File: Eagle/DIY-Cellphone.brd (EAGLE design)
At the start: 130.8 x 58.4 mm, 66 parts, among them IC1 MEGA1284, J1 ISP, U1 MCP73831, U7 M10_HDWITHOUT_EXCLUSION, X1 BU-SMA-V, X3 CCM03-3002 R102

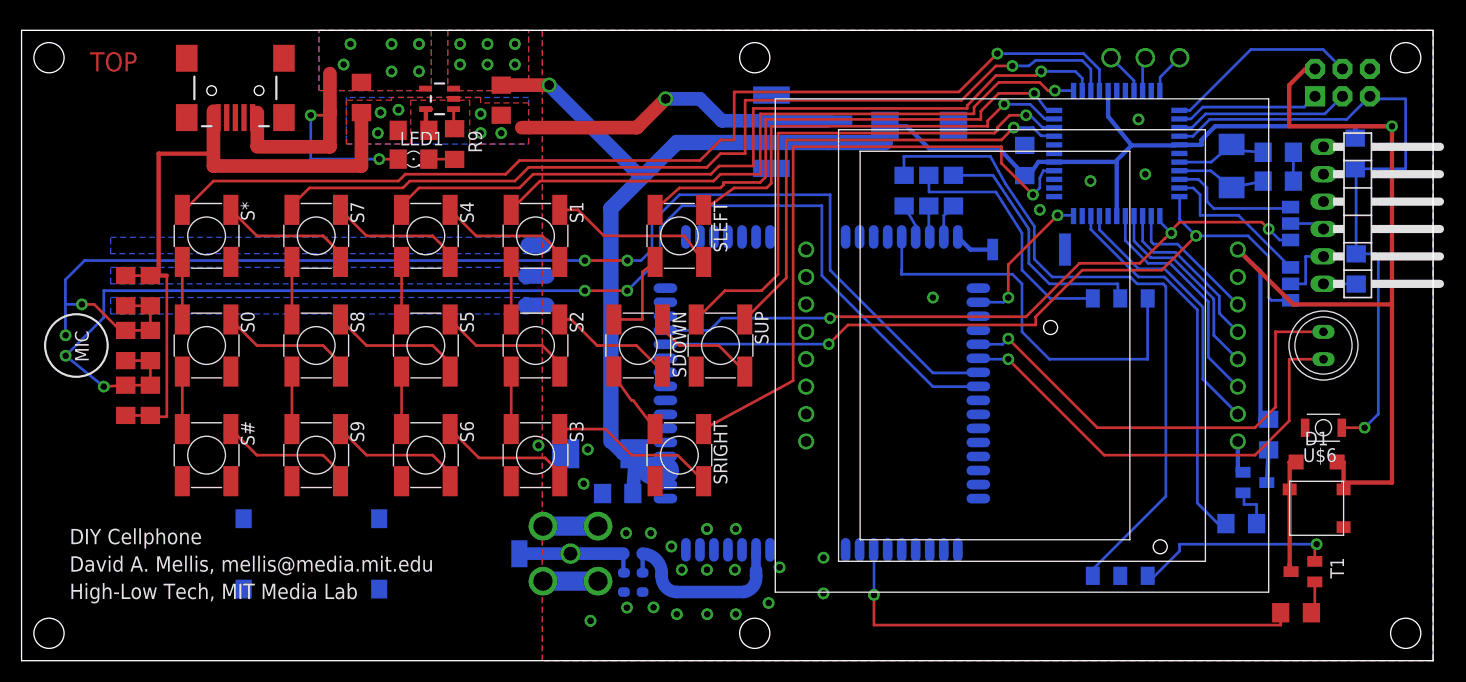
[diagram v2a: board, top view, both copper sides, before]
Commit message: Reverting to two caps. Labeling FTDI header colors.
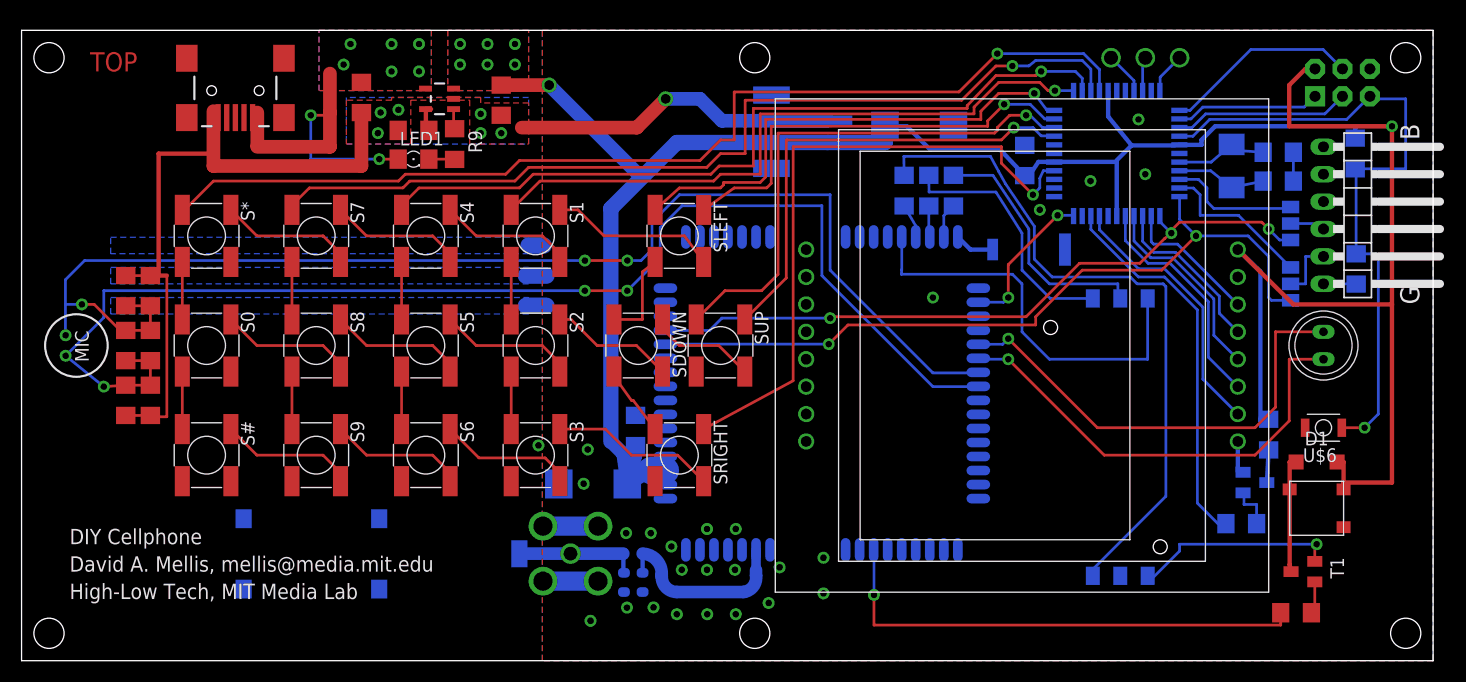
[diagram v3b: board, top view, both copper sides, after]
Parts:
- moved C13 6.07 mm to (56.9, 21.3), turned to 90 degrees
- moved C16 2.87 mm to (53.0, 16.4)
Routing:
- net VCC: track 239.2 -> 241.3 mm
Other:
- board text added: "B"
- board text added: "G"
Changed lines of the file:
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@@
 <text x="116.205" y="34.925" size="1.016" layer="26" font="fixed" rot="MR270">Cell</text>
 <text x="6.35" y="54.61" size="1.778" layer="1">TOP</text>
+<text x="129.54" y="48.26" size="1.778" layer="25" rot="R90">B</text>
+<text x="129.54" y="33.02" size="1.778" layer="25" rot="R90">G</text>
 </plain>
 <attributes>
@@
 </element>
 <element name="R4" library="rcl" package="R1206" value="10K" x="123.59" y="47.006" smashed="yes" rot="MR90">
-<attribute name="VALUE" x="121.304" y="45.609" size="1.016" layer="28" rot="MR90"/>
+<attribute name="VALUE" x="125.114" y="45.609" size="1.016" layer="28" rot="MR90"/>
 </element>
 <element name="C1" library="rcl" package="C1206" value="100 nF" x="123.679" y="36.306" smashed="yes" rot="MR90">
-<attribute name="VALUE" x="121.647" y="34.655" size="1.016" layer="28" rot="MR90"/>
+<attribute name="VALUE" x="125.457" y="34.02" size="1.016" layer="28" rot="MR90"/>
 </element>
 <element name="S1" library="cellphone" package="BUTTON_6MM_JLEAD" value="" x="47.625" y="39.37" rot="R270"/>
@@
 <attribute name="VALUE" x="86.2" y="52.305" size="1.016" layer="28" rot="MR0"/>
 </element>
-<element name="C13" library="rcl" package="C1206" value="0.1uF" x="55.245" y="15.494" smashed="yes" rot="MR0">
-<attribute name="VALUE" x="57.404" y="16.51" size="1.016" layer="28" rot="MR0"/>
+<element name="C13" library="rcl" package="C1206" value="0.1uF" x="56.896" y="21.336" smashed="yes" rot="MR90">
+<attribute name="VALUE" x="57.912" y="19.177" size="1.016" layer="28" rot="MR90"/>
 </element>
 <element name="C12" library="rcl" package="C1206" value="0.1uF" x="92.964" y="46.355" smashed="yes" rot="MR90">
@@
 <element name="U$4" library="cellphone" package="414-VA5R" value="SUPERCAPPAS" x="93.345" y="38.1" rot="MR180"/>
 <element name="8MHZ" library="fab" package="2-SMD-5X3MM" value="CRYSTAL" x="112.141" y="45.847" smashed="yes" rot="MR90">
-<attribute name="NAME" x="114.808" y="41.021" size="1.016" layer="26" rot="MR0"/>
+<attribute name="NAME" x="112.903" y="41.021" size="1.016" layer="26" rot="MR0"/>
 </element>
 <element name="C14" library="rcl" package="C1206" value="18pF" x="116.459" y="44.45" smashed="yes" rot="MR180">
@@
 <attribute name="VALUE" x="117.602" y="35.0251" size="0.02" layer="28" rot="MR270"/>
 </element>
-<element name="C16" library="rcl" package="D/7343-31R" value="1000uF" x="53.594" y="19.177" smashed="yes" rot="MR180">
-<attribute name="VALUE" x="50.579" y="22.498" size="1.016" layer="28" rot="MR180"/>
+<element name="C16" library="rcl" package="D/7343-31R" value="1000uF" x="52.959" y="16.383" smashed="yes" rot="MR180">
+<attribute name="VALUE" x="49.944" y="19.704" size="1.016" layer="28" rot="MR180"/>
 </element>
 <element name="U$5" library="cellphone" package="SPEAKER-6.4MM" value="MINI-SIREN" x="120.65" y="29.21" rot="R270"/>
@@
 <contactref element="C16" pad="+"/>
 <wire x1="54.61" y1="20.32" x2="55.753" y2="19.177" width="1.27" layer="16"/>
-<wire x1="55.753" y1="19.177" x2="56.769" y2="19.177" width="1.27" layer="16"/>
-<wire x1="56.769" y1="19.177" x2="56.896" y2="19.05" width="1.27" layer="16"/>
-<wire x1="56.896" y1="19.05" x2="56.645" y2="15.494" width="1.27" layer="16"/>
-<wire x1="56.769" y1="19.177" x2="58.322" y2="17.624" width="1.27" layer="16"/>
+<wire x1="55.753" y1="19.177" x2="56.134" y2="16.383" width="1.27" layer="16"/>
+<wire x1="56.134" y1="16.383" x2="56.896" y2="19.05" width="1.27" layer="16"/>
+<wire x1="56.896" y1="19.05" x2="56.896" y2="19.936" width="1.27" layer="16"/>
+<wire x1="56.134" y1="16.383" x2="58.322" y2="17.624" width="1.27" layer="16"/>
 <wire x1="58.322" y1="17.624" x2="59.665" y2="17.624" width="2.54" layer="16"/>
 <wire x1="59.665" y1="18.924" x2="59.665" y2="17.624" width="0.4064" layer="16"/>

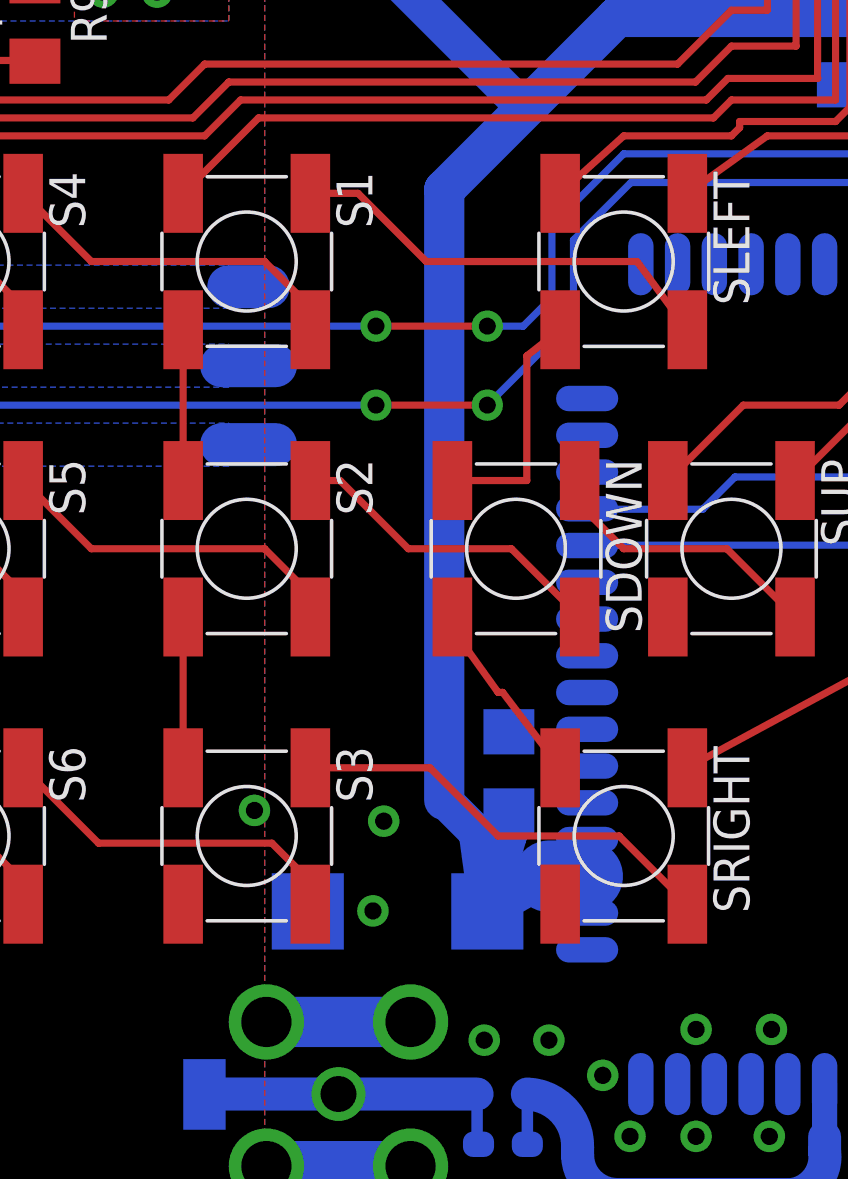
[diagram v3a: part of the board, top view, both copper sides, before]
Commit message: Moving capacitors (near the cellular module).
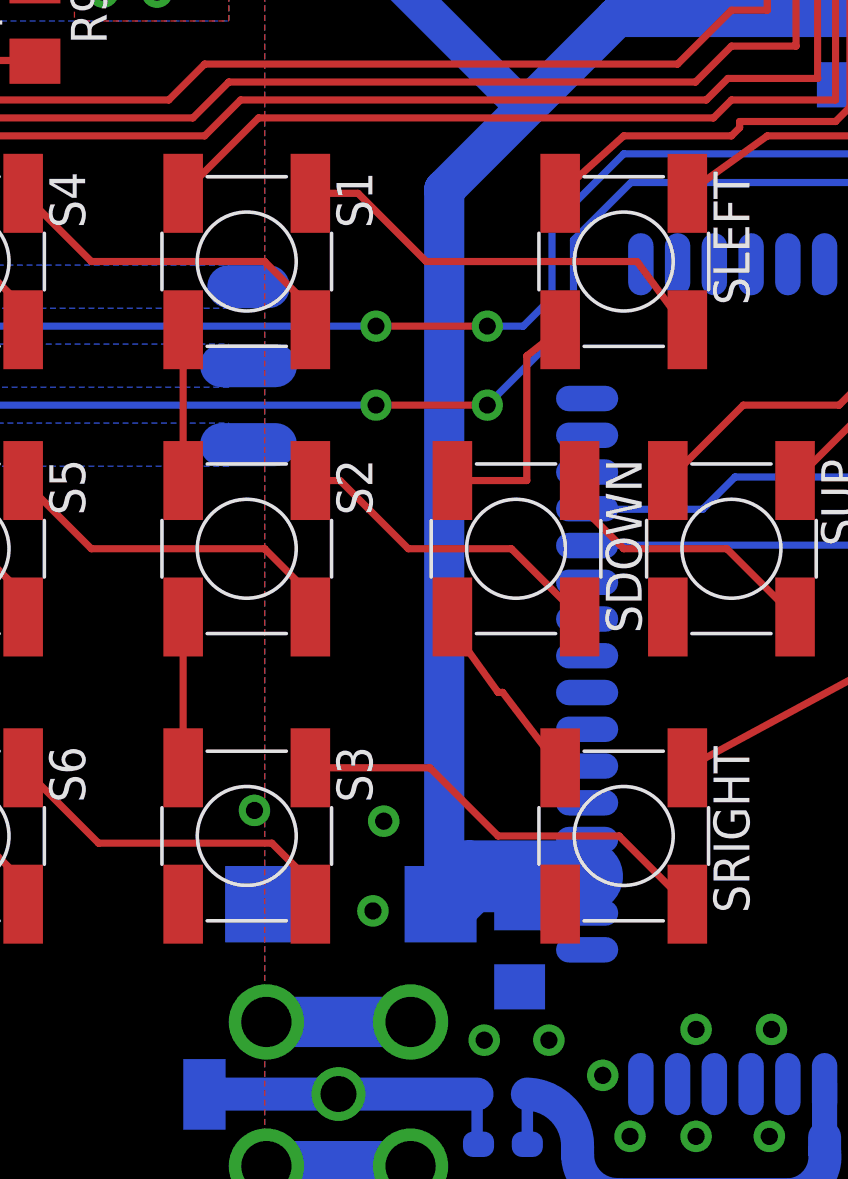
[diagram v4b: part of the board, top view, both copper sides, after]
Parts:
- moved C13 6.23 mm to (57.3, 15.1), turned to 270 degrees
- moved C16 1.67 mm to (51.3, 16.6)
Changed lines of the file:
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@@
 <attribute name="VALUE" x="86.2" y="52.305" size="1.016" layer="28" rot="MR0"/>
 </element>
-<element name="C13" library="rcl" package="C1206" value="0.1uF" x="56.896" y="21.336" smashed="yes" rot="MR90">
-<attribute name="VALUE" x="57.912" y="19.177" size="1.016" layer="28" rot="MR90"/>
+<element name="C13" library="rcl" package="C1206" value="0.1uF" x="57.277" y="15.113" smashed="yes" rot="MR270">
+<attribute name="VALUE" x="56.261" y="17.272" size="1.016" layer="28" rot="MR270"/>
 </element>
 <element name="C12" library="rcl" package="C1206" value="0.1uF" x="92.964" y="46.355" smashed="yes" rot="MR90">
@@
 <attribute name="VALUE" x="117.602" y="35.0251" size="0.02" layer="28" rot="MR270"/>
 </element>
-<element name="C16" library="rcl" package="D/7343-31R" value="1000uF" x="52.959" y="16.383" smashed="yes" rot="MR180">
-<attribute name="VALUE" x="49.944" y="19.704" size="1.016" layer="28" rot="MR180"/>
+<element name="C16" library="rcl" package="D/7343-31R" value="1000uF" x="51.308" y="16.637" smashed="yes" rot="MR180">
+<attribute name="VALUE" x="48.293" y="19.958" size="1.016" layer="28" rot="MR180"/>
 </element>
 <element name="U$5" library="cellphone" package="SPEAKER-6.4MM" value="MINI-SIREN" x="120.65" y="29.21" rot="R270"/>
@@
 <wire x1="74.693" y1="48.022" x2="60.722" y2="48.022" width="1.4224" layer="16"/>
 <wire x1="60.722" y1="48.022" x2="54.61" y2="41.91" width="1.4224" layer="16"/>
-<wire x1="54.61" y1="41.91" x2="54.61" y2="20.32" width="1.4224" layer="16"/>
+<wire x1="54.61" y1="41.91" x2="54.61" y2="16.764" width="1.4224" layer="16"/>
 <wire x1="127" y1="49.53" x2="127" y2="33.02" width="0.4064" layer="1"/>
 <wire x1="127" y1="33.02" x2="117.856" y2="33.02" width="0.4064" layer="1"/>
@@
 <wire x1="107.292" y1="47.806" x2="109.347" y2="47.806" width="0.4064" layer="16"/>
 <contactref element="C16" pad="+"/>
-<wire x1="54.61" y1="20.32" x2="55.753" y2="19.177" width="1.27" layer="16"/>
-<wire x1="55.753" y1="19.177" x2="56.134" y2="16.383" width="1.27" layer="16"/>
-<wire x1="56.134" y1="16.383" x2="56.896" y2="19.05" width="1.27" layer="16"/>
-<wire x1="56.896" y1="19.05" x2="56.896" y2="19.936" width="1.27" layer="16"/>
-<wire x1="56.134" y1="16.383" x2="58.322" y2="17.624" width="1.27" layer="16"/>
-<wire x1="58.322" y1="17.624" x2="59.665" y2="17.624" width="2.54" layer="16"/>
 <wire x1="59.665" y1="18.924" x2="59.665" y2="17.624" width="0.4064" layer="16"/>
 <wire x1="59.665" y1="17.624" x2="59.665" y2="16.324" width="0.4064" layer="16"/>
@@
 <via x="43.18" y="55.245" extent="1-16" drill="0.6"/>
 <via x="45.72" y="55.245" extent="1-16" drill="0.6"/>
+<wire x1="54.61" y1="16.764" x2="54.483" y2="16.637" width="1.4224" layer="16"/>
+<wire x1="54.61" y1="16.764" x2="55.47" y2="17.624" width="2.54" layer="16"/>
+<wire x1="55.47" y1="17.624" x2="59.665" y2="17.624" width="2.54" layer="16"/>
+<wire x1="57.277" y1="16.513" x2="58.388" y2="17.624" width="1.4224" layer="16"/>
+<wire x1="58.388" y1="17.624" x2="59.665" y2="17.624" width="1.4224" layer="16"/>
 </signal>
 <signal name="ANT" class="4">

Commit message: Add LED on M10 status pin.
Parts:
- added LED2: (no value), led:1206
- added R10: 470, rcl:R1206
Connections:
- new net N$37: LED2.C, R10.1
- net GND: now also R10.2
- net STATUS: now also LED2.A
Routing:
- net STATUS: track 3.84 -> 28.0 mm
- net N$37: track 0.00 -> 3.81 mm
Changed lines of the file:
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@@
 <element name="JP3" library="SparkFun-Connectors" package="JST-2-SMD" value="" x="70.993" y="49.022" rot="MR270"/>
 <element name="U1" library="SparkFun" package="SOT23-5" value="MCP73831" x="38.735" y="52.07" smashed="yes" rot="R90">
-<attribute name="VALUE" x="40.3225" y="54.1655" size="0.4064" layer="27" rot="R180"/>
+<attribute name="VALUE" x="41.5925" y="54.1655" size="0.8128" layer="27" rot="R180"/>
 </element>
 <element name="R7" library="rcl" package="R1206" value="2K" x="36.322" y="49.149" smashed="yes" rot="R180">
-<attribute name="VALUE" x="36.957" y="47.879" size="0.8128" layer="27" rot="R180"/>
+<attribute name="VALUE" x="36.957" y="51.054" size="0.8128" layer="27" rot="R180"/>
 </element>
 <element name="C3" library="rcl" package="C1206" value="4.7uF" x="31.496" y="52.197" smashed="yes" rot="R270">
@@
 </element>
 <element name="C4" library="rcl" package="C1206" value="4.7uF" x="44.45" y="51.943" smashed="yes" rot="R270">
-<attribute name="VALUE" x="42.545" y="53.213" size="0.8128" layer="27" rot="R270"/>
+<attribute name="VALUE" x="45.72" y="53.213" size="0.8128" layer="27" rot="R270"/>
 </element>
 <element name="U$1" library="SparkFun-Connectors" package="USB-MINIB" value="USB-MINIB-5PIN" x="19.812" y="52.832" smashed="yes" rot="R270">
@@
 <element name="U$5" library="cellphone" package="SPEAKER-6.4MM" value="MINI-SIREN" x="120.65" y="29.21" rot="R270"/>
 <element name="U$6" library="cellphone" package="B3U-1000P" value="BUTTON-2" x="120.65" y="21.59"/>
-<element name="R9" library="rcl" package="R1206" value="470" x="40.132" y="47.879" rot="R270"/>
-<element name="LED1" library="led" package="1206" value="" x="36.322" y="46.482"/>
+<element name="R9" library="rcl" package="R1206" value="470" x="40.132" y="47.879" smashed="yes" rot="R270">
+<attribute name="VALUE" x="41.402" y="48.514" size="0.8128" layer="27" rot="R270"/>
+</element>
+<element name="LED1" library="led" package="1206" value="" x="36.322" y="46.482" smashed="yes">
+<attribute name="NAME" x="35.052" y="44.577" size="0.8128" layer="25"/>
+<attribute name="VALUE" x="35.052" y="43.942" size="1.27" layer="27"/>
+</element>
+<element name="LED2" library="led" package="1206" value="" x="72.39" y="5.715" smashed="yes" rot="MR270">
+<attribute name="NAME" x="70.485" y="3.175" size="0.8128" layer="26" rot="MR180"/>
+<attribute name="VALUE" x="74.93" y="6.985" size="1.27" layer="28" rot="MR270"/>
+</element>
+<element name="R10" library="rcl" package="R1206" value="470" x="76.2" y="5.715" smashed="yes" rot="MR90">
+<attribute name="VALUE" x="74.93" y="3.175" size="0.8128" layer="28" rot="MR180"/>
+</element>
 </elements>
 <signals>
@@
 <via x="42.545" y="50.673" extent="1-16" drill="0.6"/>
 <via x="44.45" y="48.895" extent="1-16" drill="0.6"/>
+<contactref element="R10" pad="2"/>
 </signal>
 <signal name="DISP_DATA">
@@
 <wire x1="105.511" y1="52.806" x2="105.511" y2="54.076" width="0.254" layer="16"/>
 <wire x1="105.511" y1="54.076" x2="107.315" y2="55.88" width="0.254" layer="16"/>
-<wire x1="59.665" y1="21.524" x2="105.492" y2="52.806" width="0" layer="19" extent="16-16"/>
+<contactref element="LED2" pad="A"/>
+<wire x1="59.665" y1="21.524" x2="67.376" y2="21.524" width="0.254" layer="16"/>
+<wire x1="67.376" y1="21.524" x2="72.39" y2="16.51" width="0.254" layer="16"/>
+<wire x1="72.39" y1="16.51" x2="72.39" y2="7.137" width="0.254" layer="16"/>
+<wire x1="72.39" y1="16.51" x2="105.492" y2="52.806" width="0" layer="19" extent="16-16"/>
 </signal>
 <signal name="SIM_RSTR">
@@
 <wire x1="40.132" y1="46.482" x2="40.132" y2="46.457" width="0.254" layer="1"/>
 </signal>
+<signal name="N$37">
+<contactref element="LED2" pad="C"/>
+<contactref element="R10" pad="1"/>
+<wire x1="72.39" y1="4.293" x2="76.2" y2="4.293" width="0.254" layer="16"/>
+</signal>
 </signals>
